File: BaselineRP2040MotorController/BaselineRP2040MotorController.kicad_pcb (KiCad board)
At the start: 2 copper layers, 179 parts, among them J1 CPU1 USB, J2 Encoder 1, J5 Conn_01x06, Q1 Q_PNP_BEC, Q2 Q_PNP_BEC, Q3 Q_PNP_BEC, SW1 KT11B2SAM34LFS, U1 USBLC6-4SC6, U10 INA240A1D, U11 USBLC6-4SC6, U12 TLV1117LV33DCYR, U13 TX4139, U14 MT2492, U17 ADC081S021CISD/NOPB, U2 W25Q128JVSIQ, U3 RP2040, U4 USBLC6-2P6, U5 EG3113, U6 INA240A1D, U7 EG3113, U8 INA240A1D, U9 EG3113, Y1 12MHz

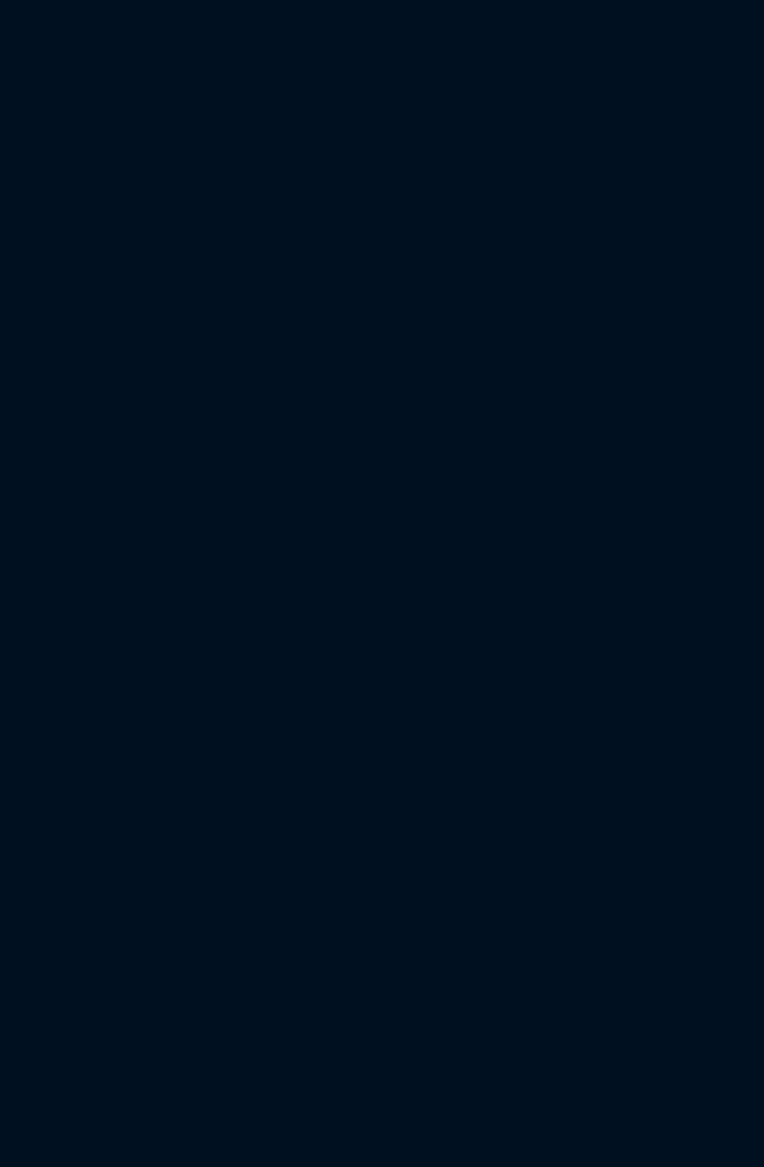
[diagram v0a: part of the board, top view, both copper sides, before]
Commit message: Change Mosfet Footprint.
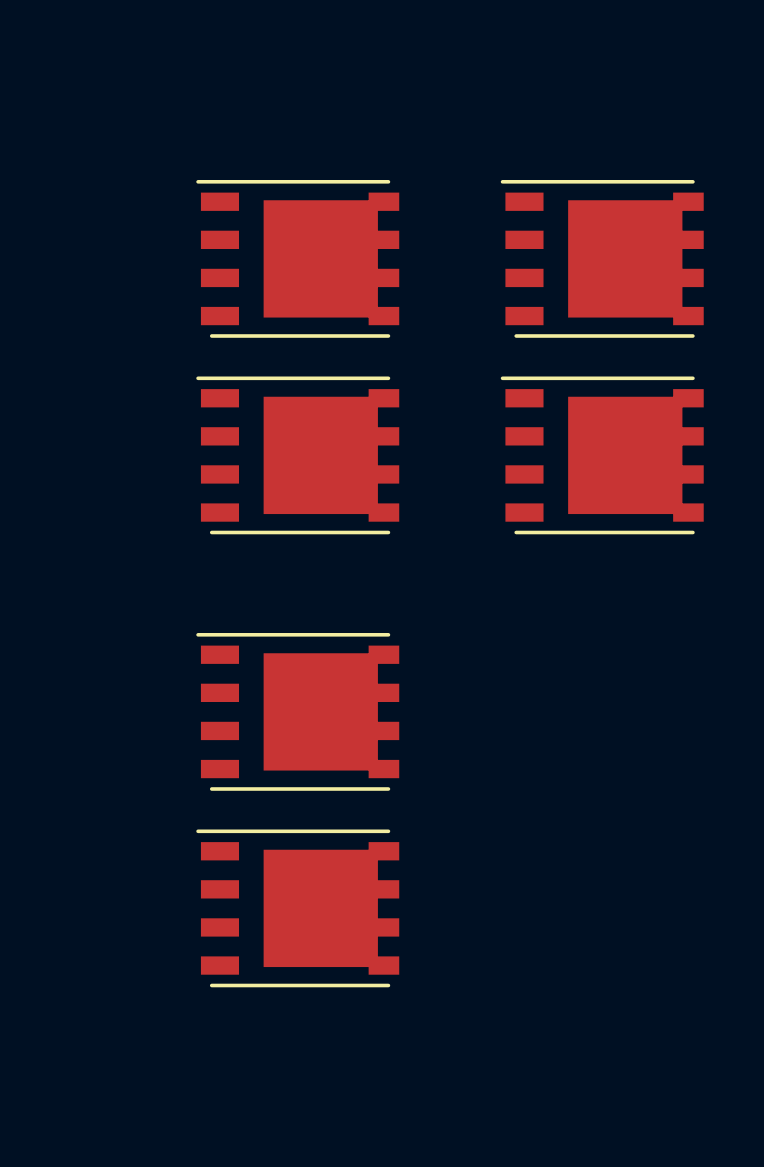
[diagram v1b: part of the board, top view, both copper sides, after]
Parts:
- added AH1: MOSFETSO-8, [EastMakes] Mosfets:PowerPAK_SO-8_123, F.Cu at (224.5, 77.4)
- added AH2: MOSFETSO-8, [EastMakes] Mosfets:PowerPAK_SO-8_123, F.Cu at (214.4, 92.5)
- added AH3: MOSFETSO-8, [EastMakes] Mosfets:PowerPAK_SO-8_123, F.Cu at (214.4, 77.4)
- added AL1: MOSFETSO-8, [EastMakes] Mosfets:PowerPAK_SO-8_123, F.Cu at (224.5, 83.9)
- added AL2: MOSFETSO-8, [EastMakes] Mosfets:PowerPAK_SO-8_123, F.Cu at (214.4, 99.0)
- added AL3: MOSFETSO-8, [EastMakes] Mosfets:PowerPAK_SO-8_123, F.Cu at (214.4, 83.9)

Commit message: Continue Work
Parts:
- removed J2: Encoder 1, RJ14 Footprint:RJ14_Connfly_DS1133-S6_Horizontal
- moved AH1 111.5 mm to (113.5, 87.5)
- moved AL1 111.5 mm to (113.5, 94.1)
- moved AH2 103.4 mm to (113.5, 115.2)
- moved AL2 103.4 mm to (113.5, 121.8)
- moved AH3 102.4 mm to (113.5, 59.8)
- moved AL3 102.4 mm to (113.5, 66.4)
- moved U5 58.7 mm to (105.2, 87.6)
- moved U6 58.7 mm to (105.2, 94.2)
- moved D3 48.3 mm to (124.3, 92.2)
- moved D4 48.3 mm to (124.3, 94.6)
- moved R21 47.2 mm to (117.4, 74.2)
- moved R22 47.2 mm to (117.4, 79.0)
- moved R11 45.3 mm to (107.0, 73.0)
- moved R12 45.3 mm to (107.0, 75.5)
- moved R13 45.3 mm to (107.0, 78.0)
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
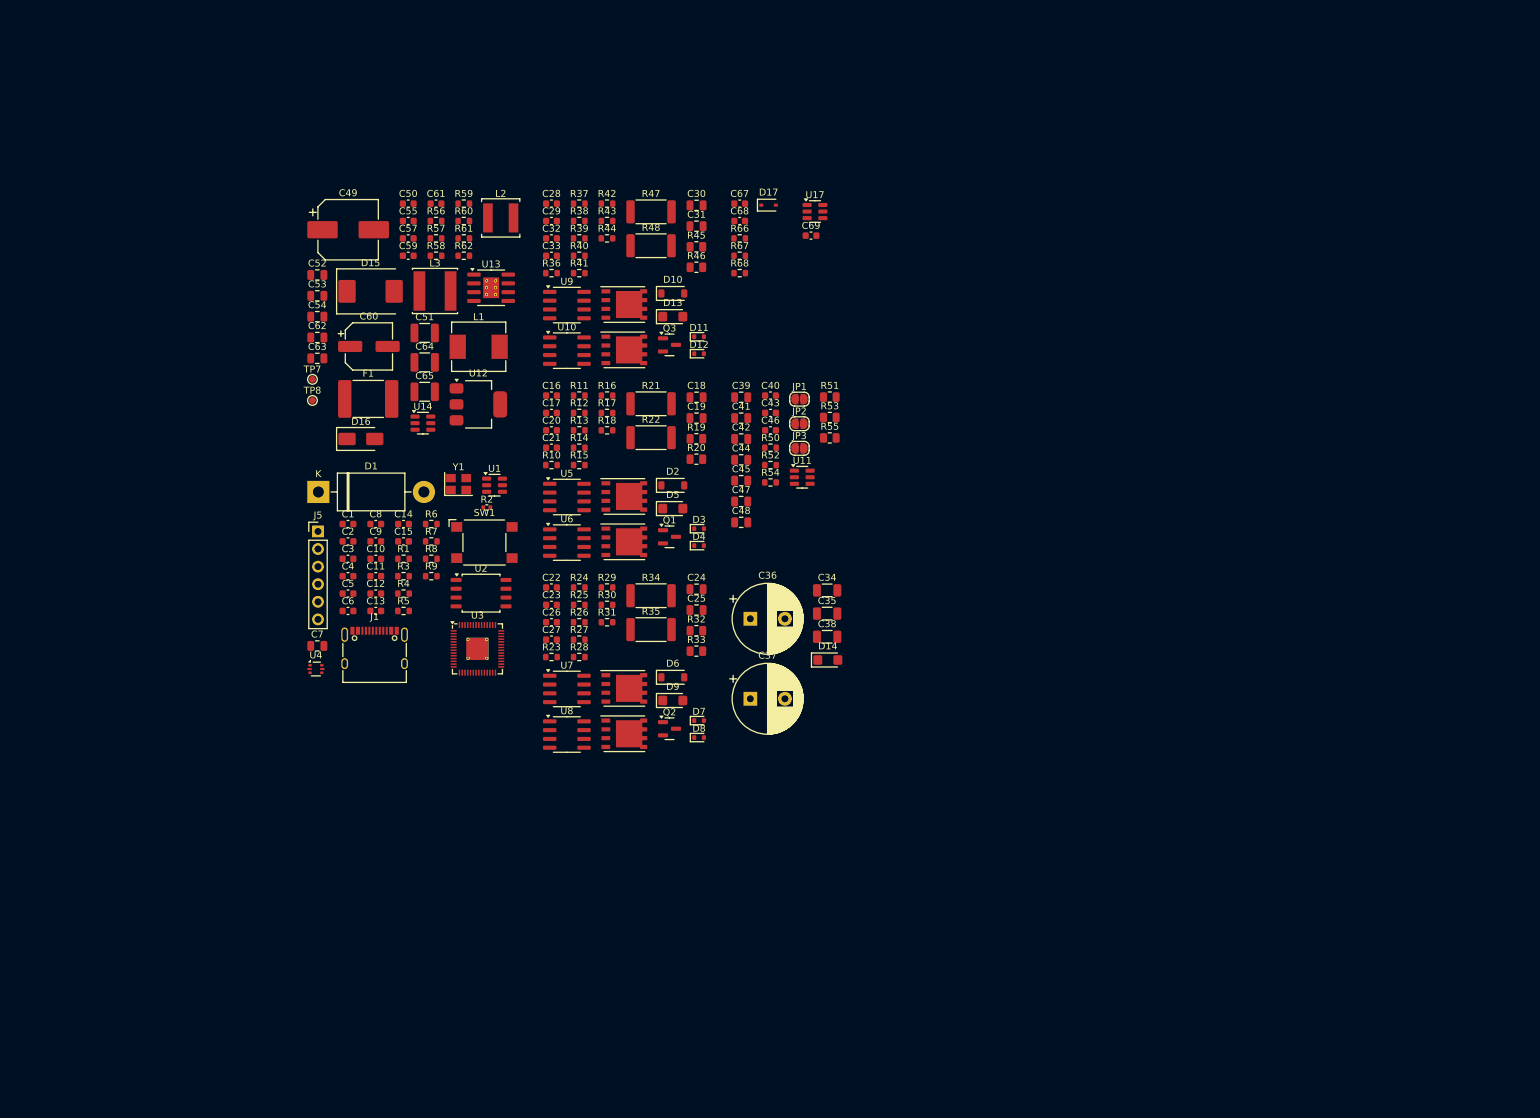
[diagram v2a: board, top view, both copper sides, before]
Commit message: Drop some features.
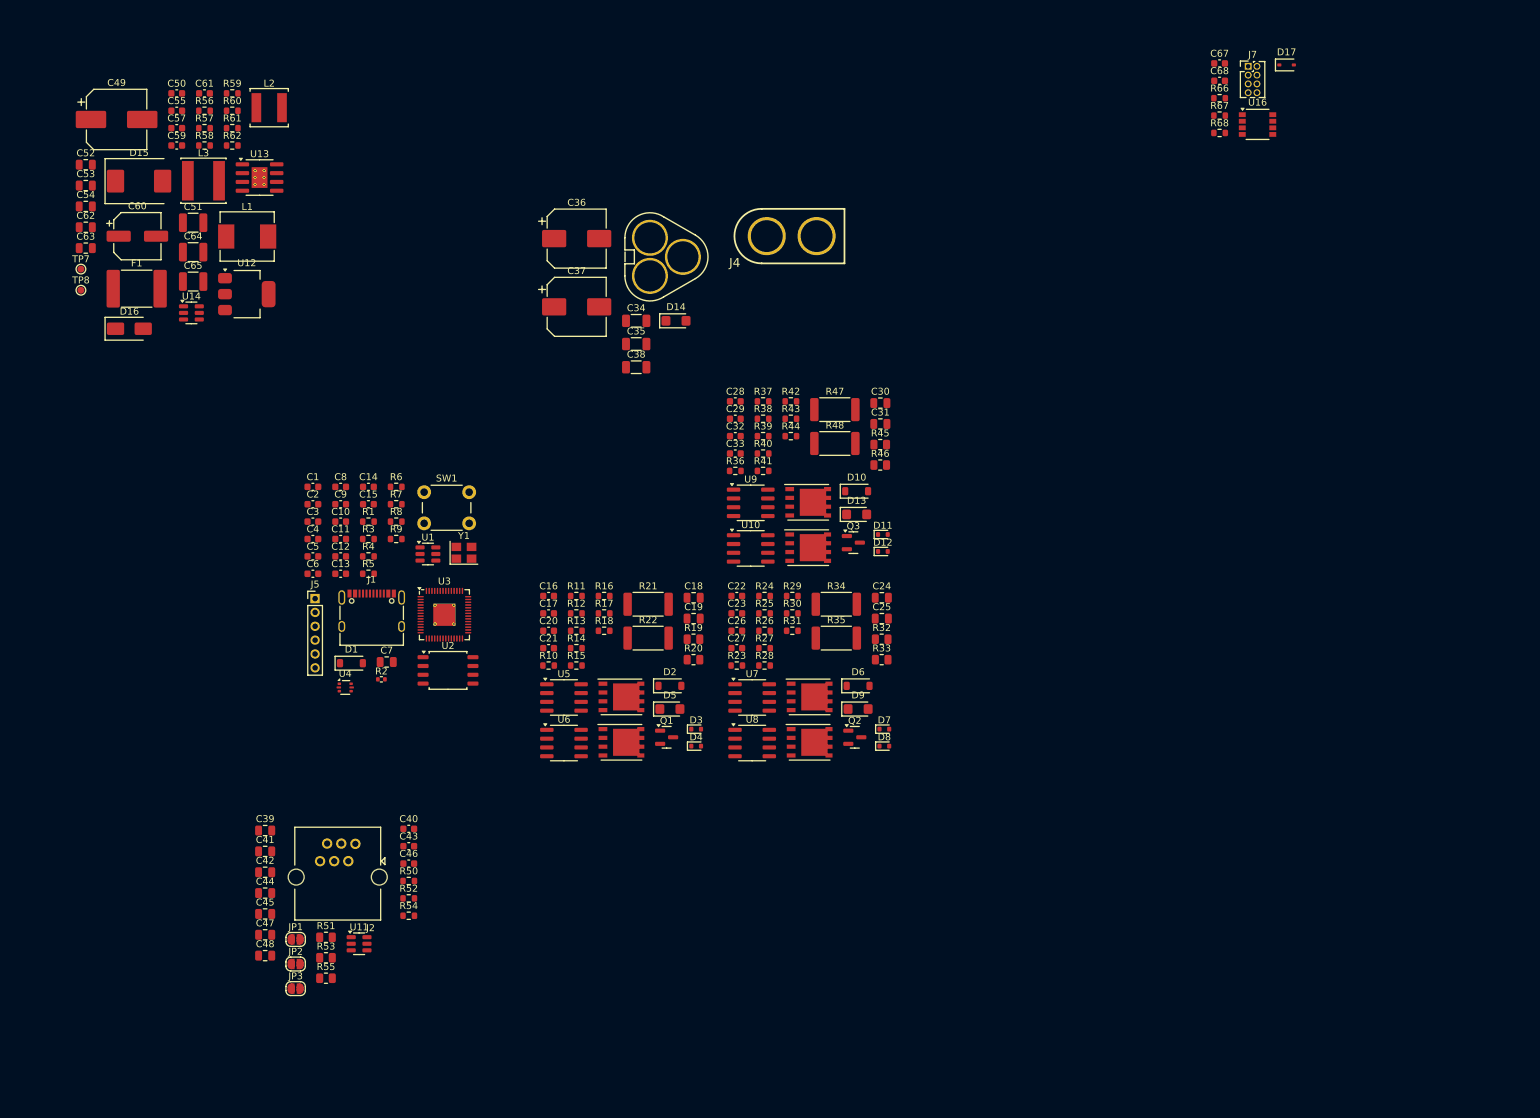
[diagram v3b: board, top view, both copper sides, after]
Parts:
- removed C69: 1u, Capacitor_SMD:C_0603_1608Metric
- removed U17: ADC081S021CISD/NOPB, Package_TO_SOT_SMD:SOT-23-6
- added J2: Encoder 1, [EastMakes] Connectors:RJ14_Connfly_DS1133-S6_Horizontal, F.Cu at (65.9, 148.7)
- added J3: Conn_01x03, [EastMakes] Connectors:MT60-F.G.Y, F.Cu at (117.2, 52.9)
- added J4: XT60 Power Connector, [EastMakes] Connectors:CONN-TH_XT60UPB-M, F.Cu at (137.7, 49.9)
- added J7: Conn_02x04_Odd_Even, Connector_PinHeader_1.27mm:PinHeader_2x04_P1.27mm_Vertical, F.Cu at (203.6, 25.4)
- added U16: ADS7822U, Package_TO_SOT_SMD:SuperSOT-8, F.Cu at (204.9, 33.8)
- C36, C37: footprint Capacitor_THT:CP_Radial_D10.0mm_P5.00mm -> Capacitor_SMD:CP_Elec_8x10
- D1: footprint Diode_THT:D_DO-201AD_P15.24mm_Horizontal -> Diode_SMD:D_SOD-123
- J5: footprint Connector_PinHeader_2.54mm:PinHeader_1x06_P2.54mm_Vertical -> Connector_PinHeader_2.00mm:PinHeader_1x06_P2.00mm_Vertical
- SW1: footprint Button_Switch_SMD:SW_SPST_Omron_B3FS-100xP -> Button_Switch_THT:SW_PUSH_6mm_H9.5mm
- moved JP3 106.7 mm to (66.1, 158.6)
- moved JP1 106.7 mm to (66.1, 151.5)
- moved JP2 106.7 mm to (66.1, 155.0)
- moved R51 106.7 mm to (70.4, 151.2)
- moved R55 106.7 mm to (70.4, 157.1)
- moved R53 106.7 mm to (70.4, 154.1)
- moved C41 92.9 mm to (61.7, 138.8)
- moved C45 92.9 mm to (61.7, 147.8)
- moved C39 92.9 mm to (61.7, 135.8)
- moved C42 92.9 mm to (61.7, 141.8)
- moved C44 92.9 mm to (61.7, 144.8)
- moved C47 92.9 mm to (61.7, 150.8)
- moved C48 92.9 mm to (61.7, 153.8)
- moved U11 92.9 mm to (75.2, 152.1)
- moved C43 81.5 mm to (82.4, 138.0)
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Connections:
- net Net-(D17-A) renamed /Voltage Sensing/TestVoltage

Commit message: Erhhhhrh
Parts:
- removed C1, C10, C12, C13, C14, C15, C4, C5, C68, C8, C9: 100n, Capacitor_SMD:C_0603_1608Metric
- removed C11, C50, C6, C67: 1u, Capacitor_SMD:C_0603_1608Metric
- removed C2, C3: 20p, Capacitor_SMD:C_0603_1608Metric
- removed C53, C7: 10u, Capacitor_SMD:C_0805_2012Metric
- removed C54, C63: 22uF 25V, Capacitor_SMD:C_0805_2012Metric
- removed C59: 22nF, Capacitor_SMD:C_0603_1608Metric
- removed C61: 22pF, Capacitor_SMD:C_0603_1608Metric
- removed C62: 47uF 10v, Capacitor_SMD:C_0805_2012Metric
- removed D1: B5819W SL, Diode_SMD:D_SOD-123
- removed D17: 1N4148WS, Diode_SMD:D_SOD-323
- removed J1: CPU1 USB, Connector_USB:USB_C_Receptacle_XKB_U262-16XN-4BVC11
- removed J5: Conn_01x06, Connector_PinHeader_2.00mm:PinHeader_1x06_P2.00mm_Vertical
- removed J7: Conn_02x04_Odd_Even, Connector_PinHeader_1.27mm:PinHeader_2x04_P1.27mm_Vertical
- removed L2: 10uH, Inductor_SMD:L_Sunlord_SWPA5040S
- removed R1, R5: 1.1k, Resistor_SMD:R_0603_1608Metric
- removed R2: DNF, Resistor_SMD:R_0402_1005Metric
- removed R3, R4, R8, R9: 5.1k, Resistor_SMD:R_0603_1608Metric
- removed R6, R7: 27R, Resistor_SMD:R_0603_1608Metric
- removed R60: 110k 0.1%, Resistor_SMD:R_0603_1608Metric
- removed R61: 15k 0.1%, Resistor_SMD:R_0603_1608Metric
- removed R62: 100k, Resistor_SMD:R_0603_1608Metric
- removed R66, R67: 50k 0.1%, Resistor_SMD:R_0603_1608Metric
- removed R68: 5.1k 0.1%, Resistor_SMD:R_0603_1608Metric
- removed SW1: KT11B2SAM34LFS, Button_Switch_THT:SW_PUSH_6mm_H9.5mm
- removed U12: TLV1117LV33DCYR, Package_TO_SOT_SMD:SOT-223-3_TabPin2
- removed U14: MT2492, Package_TO_SOT_SMD:SOT-23-6
- removed U16: ADS7822U, Package_TO_SOT_SMD:SuperSOT-8
- removed U2: W25Q128JVSIQ, Package_SO:SOIC-8_5.23x5.23mm_P1.27mm
- removed U3: RP2040, Package_DFN_QFN:QFN-56-1EP_7x7mm_P0.4mm_EP3.2x3.2mm_ThermalVias
- removed U4: USBLC6-2P6, Package_TO_SOT_SMD:SOT-666
- removed Y1: 12MHz, Crystal:Crystal_SMD_3225-4Pin_3.2x2.5mm
- U1: value USBLC6-4SC6 -> Pico; footprint Package_TO_SOT_SMD:SOT-23-6 -> [EastMakes] PiPico:RPi_Pico_SMD_TH
- moved R59 146.2 mm to (97.3, 169.8)
- moved C52 141.3 mm to (118.6, 154.0)
- moved TP8 138.7 mm to (111.7, 173.3)
- moved TP7 138.7 mm to (111.7, 170.3)
- moved R57 137.8 mm to (97.3, 164.8)
- moved R56 137.8 mm to (97.3, 162.3)
- moved R58 137.8 mm to (97.3, 167.3)
- moved D16 134.9 mm to (119.9, 173.5)
- moved C55 134.4 mm to (97.3, 157.2)
- moved C57 134.4 mm to (97.3, 159.8)
- moved C60 132.9 mm to (104.5, 167.8)
- moved D15 132.9 mm to (104.8, 159.9)
- moved C51 126.3 mm to (113.0, 158.1)
- moved L1 126.3 mm to (120.8, 160.1)
- moved U13 123.3 mm to (120.6, 149.3)
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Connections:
- net /BLDC Power Control/X_SENSE renamed /BLDC Power Control/Motor Phase X/X_SENSE
- C39 pad 2: /Hall Effect Encoders/ENC1_RX -> /Encoder RX
- C40 pad 2: /Hall Effect Encoders/ENC1_RX -> /Encoder RX
- C41 pad 2: /Hall Effect Encoders/ENC1_RX -> /Encoder RX
- C42 pad 1: /Hall Effect Encoders/ENC1_CS -> /Encoder CS
- C43 pad 2: /Hall Effect Encoders/ENC1_CS -> /Encoder CS
- C44 pad 2: /Hall Effect Encoders/ENC1_CS -> /Encoder CS
- C45 pad 1: /Hall Effect Encoders/ENC1_SCK -> /Encoder SCK
- C46 pad 2: /Hall Effect Encoders/ENC1_SCK -> /Encoder SCK
- C47 pad 2: /Hall Effect Encoders/ENC1_SCK -> /Encoder SCK
- J2 pad 3: /Hall Effect Encoders/ENC1_RX -> /Encoder RX
- J2 pad 4: /Hall Effect Encoders/ENC1_CS -> /Encoder CS
- J2 pad 5: /Hall Effect Encoders/ENC1_SCK -> /Encoder SCK
- R50 pad 2: /Hall Effect Encoders/ENC1_RX -> /Encoder RX
- R51 pad 2: /Hall Effect Encoders/ENC1_RX -> /Encoder RX
- R52 pad 2: /Hall Effect Encoders/ENC1_CS -> /Encoder CS
- R53 pad 2: /Hall Effect Encoders/ENC1_CS -> /Encoder CS
- R54 pad 2: /Hall Effect Encoders/ENC1_SCK -> /Encoder SCK
- R55 pad 2: /Hall Effect Encoders/ENC1_SCK -> /Encoder SCK
- U1 pad 1: /RaspberryPiPico/SWD -> unconnected-(U1-GPIO0-Pad1)
- U1 pad 2: GND -> unconnected-(U1-GPIO1-Pad2)
- U1 pad 3: /RaspberryPiPico/GPIO25 -> unconnected-(U1-GND-Pad3)
- U1 pad 4: /RaspberryPiPico/SWCLK -> unconnected-(U1-GPIO2-Pad4)
- U1 pad 5: +3V3 -> unconnected-(U1-GPIO3-Pad5)
- U1 pad 6: /RaspberryPiPico/GPIO24 -> /BLDC Power Control/PWM_H_U
- U11 pad 3: /Hall Effect Encoders/ENC1_CS -> /Encoder CS
- U11 pad 4: /Hall Effect Encoders/ENC1_RX -> /Encoder RX
- U11 pad 6: /Hall Effect Encoders/ENC1_SCK -> /Encoder SCK
- U6 pad 5: /BLDC Power Control/U_SENSE -> /CurrentSense2
- U8 pad 5: /BLDC Power Control/V_SENSE -> /CurrentSense1
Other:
- board outline added: 125 x 75 mm

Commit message: Going to take a break.
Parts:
- removed U1: Pico, [EastMakes] PiPico:RPi_Pico_SMD_TH
- moved C51 126.1 mm to (61.8, 42.9)
- moved C52 126.1 mm to (67.4, 38.8)
- moved C55 126.1 mm to (46.1, 42.1)
- moved C60 126.1 mm to (53.3, 52.6)
- moved D15 126.1 mm to (53.5, 44.7)
- moved L1 126.1 mm to (69.6, 44.9)
- moved R57 126.1 mm to (46.1, 49.6)
- moved R58 126.1 mm to (46.1, 52.1)
- moved TP8 126.1 mm to (60.5, 58.1)
- moved C57 126.1 mm to (46.1, 44.6)
- moved D16 126.1 mm to (68.7, 58.3)
- moved R56 126.1 mm to (46.1, 47.1)
- moved R59 126.1 mm to (46.1, 54.6)
- moved TP7 126.1 mm to (60.5, 55.1)
- moved U13 126.1 mm to (69.4, 34.1)
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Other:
- board outline removed
